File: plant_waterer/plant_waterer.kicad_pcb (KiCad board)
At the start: 2 copper layers, 59.1 x 41.3 mm, 20 parts, among them J1 PJ-002AH, J2 Conn_01x02, J3 Conn_01x03, U1 XIAO_RP2040, U2 TB6612FNG,C,8,EL, U3 OLED_DISP, U4 AP2204R-5.0TRG1

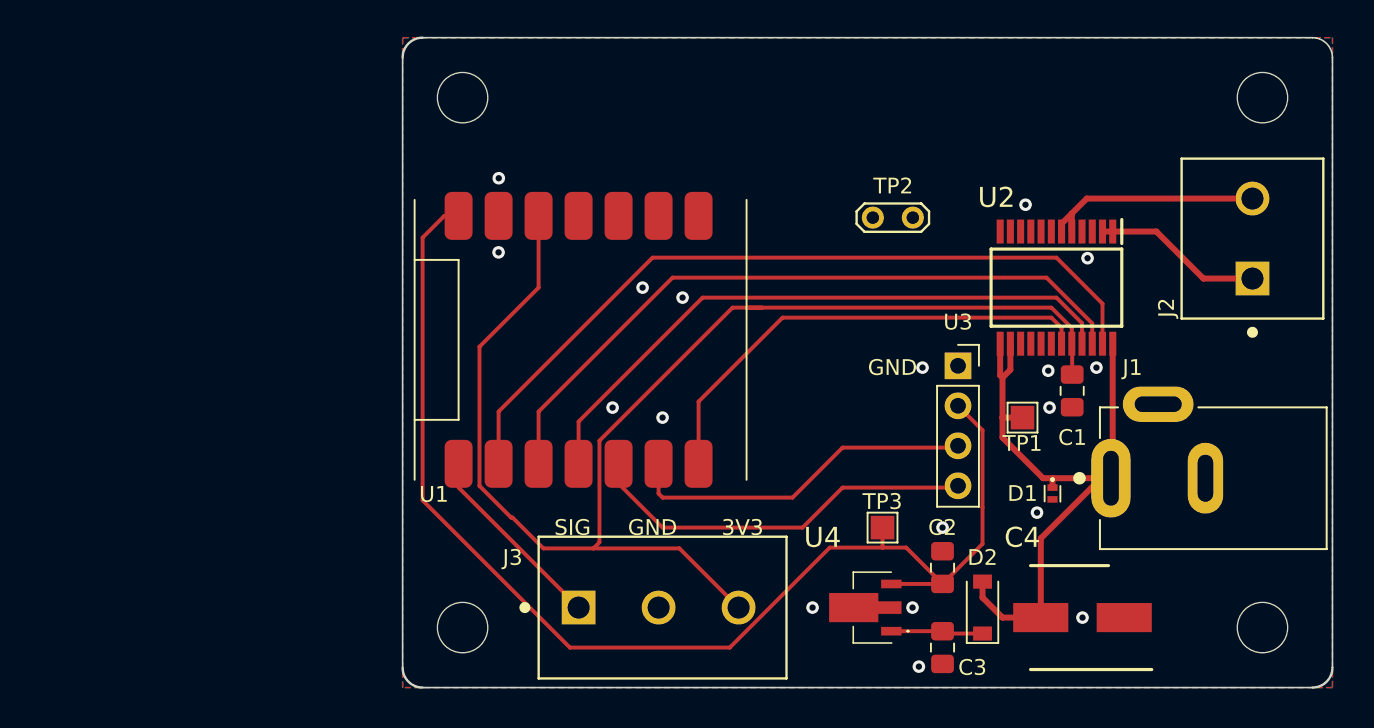
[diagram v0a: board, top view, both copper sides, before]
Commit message: Added UART input Added second motor output Added fuse and reverse polarity protection
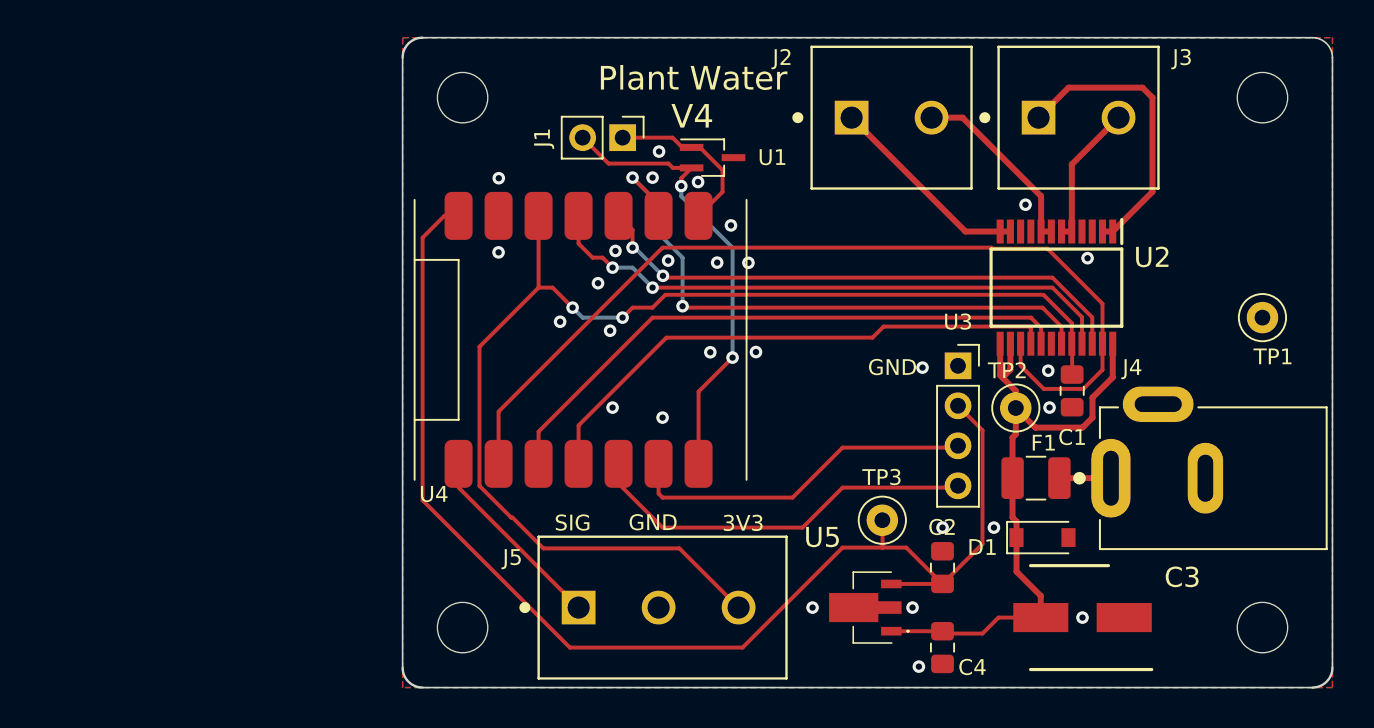
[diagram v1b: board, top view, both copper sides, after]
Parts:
- removed D2: D, Diode_SMD:D_SOD-123
- added F1: Polyfuse_Small, Fuse:Fuse_1210_3225Metric_Pad1.42x2.65mm_HandSolder, F.Cu at (101.2, 62.9)
- added J1: Conn_01x02, Connector_PinHeader_2.54mm:PinHeader_1x02_P2.54mm_Vertical, F.Cu at (74.9, 41.3)
- added J2: Conn_01x02, Library:CONN 1x2 5mm, F.Cu at (94.8, 40.0)
- added U1: ESD7002, Package_TO_SOT_SMD:SOT-323_SC-70_Handsoldering, F.Cu at (80.6, 42.5)
- D1: value SP3130-01ETG -> TV02W480-G; footprint Library:SP3130-01ETG -> Diode_SMD:D_SOD-123
- TP1: renamed from TP2; footprint TestPoint:TestPoint_2Pads_Pitch2.54mm_Drill0.8mm -> TestPoint:TestPoint_Loop_D1.80mm_Drill1.0mm_Beaded
- TP2: renamed from TP1; footprint TestPoint:TestPoint_Pad_1.5x1.5mm -> TestPoint:TestPoint_Loop_D1.80mm_Drill1.0mm_Beaded
- TP3: footprint TestPoint:TestPoint_Pad_1.5x1.5mm -> TestPoint:TestPoint_Loop_D1.80mm_Drill1.0mm_Beaded
- moved TP1 25.5 mm to (115.6, 52.7)
- moved J3 9.59 mm to (106.7, 40.0), turned to 0 degrees
- moved D1 3.24 mm to (101.6, 66.7), turned to 0 degrees
- moved TP2 0.74 mm to (99.9, 58.4)
- moved TP3 0.47 mm to (91.4, 65.6)
- renumbered C4 to C3, C3 to C4, J2 to J3, J1 to J4, J3 to J5, U1 to U4, U4 to U5
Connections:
- C4 pad 2: Net-(D2-Pad1) -> +12V
- J4 pad 1: +12V -> Net-(J1-Pad1)
- U2 pad 11: unconnected-(U3-Pad11) -> /B01
- U2 pad 12: unconnected-(U3-Pad12) -> /B01
- U2 pad 15: unconnected-(U3-Pad15) -> /PWMA
- U2 pad 16: unconnected-(U3-Pad16) -> /BIN2
- U2 pad 17: unconnected-(U3-Pad17) -> /BIN1
- U2 pad 7: unconnected-(U3-Pad7) -> /BO2
- U2 pad 8: unconnected-(U3-Pad8) -> /BO2
- U4 pad 10: unconnected-(U1-Pad10) -> /AIN1
- U4 pad 2: /AIN2 -> /BIN1
- U4 pad 3: /AIN1 -> /BIN2
- U4 pad 6: /STBY -> Net-(U1-Pad6)
- U4 pad 7: unconnected-(U1-Pad7) -> Net-(U1-Pad7)
- U4 pad 8: unconnected-(U1-Pad8) -> /STBY
- U4 pad 9: unconnected-(U1-Pad9) -> /AIN2
- U5 pad 1: Net-(D2-Pad1) -> +12V
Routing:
- net /BIN1: track 0.00 -> 38.2 mm
- net /BIN2: track 0.00 -> 34.8 mm
- net Net-(U1-Pad6): track 0.00 -> 29.0 mm, vias 0 -> 2
- net /B01: track 0.00 -> 13.1 mm
- net /BO2: track 0.00 -> 11.9 mm
- net /PWMA: track 49.5 -> 59.4 mm
- net Net-(U1-Pad7): track 0.00 -> 9.62 mm
- net /AIN2: track 44.5 -> 35.1 mm, vias 0 -> 2
- net /AO1: track 10.8 -> 18.5 mm
- net /STBY: track 30.5 -> 37.5 mm, vias 0 -> 2
- net Net-(D2-Pad1): track 5.85 -> 0.00 mm
- net +3.3V: track 83.4 -> 77.6 mm, vias 0 -> 2
- net /AO2: track 14.0 -> 9.11 mm
- net Net-(J1-Pad1): track 0.00 -> 3.27 mm
- net /AIN1: track 39.9 -> 37.4 mm, vias 0 -> 2
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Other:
- board text added: "Plant Water V4"

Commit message: Updated version to latest
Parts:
- moved TP1 3.42 mm to (112.4, 51.4)
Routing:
- net GND: vias 28 -> 35
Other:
- board text added: "12V 250mA"
- board text added: "Plant Water V5"
- board text removed: "Plant Water V4"
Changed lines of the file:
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@@
     (fp_line (start 1.6 1.25) (end -1.6 1.25) (layer "F.Fab") (width 0.1))
     (fp_line (start 1.6 -1.25) (end 1.6 1.25) (layer "F.Fab") (width 0.1))
-    (pad "1" smd roundrect (at -1.4875 0 180) (size 1.425 2.65) (layers "F.Cu" "F.Paste" "F.Mask") (roundrect_rratio 0.175439)
+    (pad "1" smd roundrect (at -1.4875 0 180) (size 1.425 2.65) (layers "F.Cu" "F.Paste" "F.Mask") (roundrect_rratio 0.1754392982)
       (net 16 "Net-(J1-Pad1)") (pintype "passive"))
-    (pad "2" smd roundrect (at 1.4875 0 180) (size 1.425 2.65) (layers "F.Cu" "F.Paste" "F.Mask") (roundrect_rratio 0.175439)
+    (pad "2" smd roundrect (at 1.4875 0 180) (size 1.425 2.65) (layers "F.Cu" "F.Paste" "F.Mask") (roundrect_rratio 0.1754392982)
       (net 3 "+12V") (pintype "passive"))
     (model "${KICAD6_3DMODEL_DIR}/Fuse.3dshapes/Fuse_1210_3225Metric.wrl"
@@
   )
   (footprint "TestPoint:TestPoint_Loop_D1.80mm_Drill1.0mm_Beaded" (layer "F.Cu")
-    (at 115.57 52.705)
+    (at 112.395 51.435)
     (descr "wire loop with bead as test point, loop diameter 1.8mm, hole diameter 1.0mm")
     (tags "test point wire loop bead")
@@
     (effects (font (size 1 1) (thickness 0.15)))
   )
-  (gr_text "Plant Water\nV4" (at 79.375 38.735) (layer "F.SilkS")
+  (gr_text "Plant Water\nV5" (at 79.375 38.735) (layer "F.SilkS")
     (effects (font (size 1.5 1.5) (thickness 0.3)))
   )
   (gr_text "GND" (at 92.075 55.88) (layer "F.SilkS")
+    (effects (font (size 1 1) (thickness 0.15)))
+  )
+  (gr_text "12V 250mA" (at 118.745 53.34 90) (layer "F.SilkS")
     (effects (font (size 1 1) (thickness 0.15)))
   )
@@
   (via (at 93.748867 74.869654) (size 0.8) (drill 0.4) (layers "F.Cu" "B.Cu") (free) (net 1))
   (via (at 101.964058 56.077174) (size 0.8) (drill 0.4) (layers "F.Cu" "B.Cu") (free) (net 1))
+  (via (at 96.816593 74.839758) (size 0.8) (drill 0.4) (layers "F.Cu" "B.Cu") (free) (net 1))
   (via (at 102.046359 58.416855) (size 0.8) (drill 0.4) (layers "F.Cu" "B.Cu") (free) (net 1))
   (via (at 86.995 71.12) (size 0.8) (drill 0.4) (layers "F.Cu" "B.Cu") (free) (net 1))
@@
   (via (at 76.835 43.815) (size 0.8) (drill 0.4) (layers "F.Cu" "B.Cu") (free) (net 1))
   (via (at 74.4806 48.471006) (size 0.8) (drill 0.4) (layers "F.Cu" "B.Cu") (free) (net 1))
+  (via (at 100.539658 48.699476) (size 0.8) (drill 0.4) (layers "F.Cu" "B.Cu") (free) (net 1))
   (via (at 79.725295 44.093377) (size 0.8) (drill 0.4) (layers "F.Cu" "B.Cu") (free) (net 1))
   (via (at 77.47 59.055) (size 0.8) (drill 0.4) (layers "F.Cu" "B.Cu") (free) (net 1))
+  (via (at 104.450136 45.525972) (size 0.8) (drill 0.4) (layers "F.Cu" "B.Cu") (free) (net 1))
+  (via (at 82.169779 41.568877) (size 0.8) (drill 0.4) (layers "F.Cu" "B.Cu") (free) (net 1))
+  (via (at 101.902302 66.685827) (size 0.8) (drill 0.4) (layers "F.Cu" "B.Cu") (free) (net 1))
   (via (at 67.053675 48.560428) (size 0.8) (drill 0.4) (layers "F.Cu" "B.Cu") (free) (net 1))
   (via (at 83.40105 54.8908) (size 0.8) (drill 0.4) (layers "F.Cu" "B.Cu") (free) (net 1))
@@
   (via (at 82.92496 49.223992) (size 0.8) (drill 0.4) (layers "F.Cu" "B.Cu") (free) (net 1))
   (via (at 93.345 71.12) (size 0.8) (drill 0.4) (layers "F.Cu" "B.Cu") (free) (net 1))
+  (via (at 104.414032 66.700867) (size 0.8) (drill 0.4) (layers "F.Cu" "B.Cu") (free) (net 1))
   (via (at 77.247722 42.158226) (size 0.8) (drill 0.4) (layers "F.Cu" "B.Cu") (free) (net 1))
+  (via (at 82.2149 43.554196) (size 0.8) (drill 0.4) (layers "F.Cu" "B.Cu") (free) (net 1))
   (via (at 73.370251 50.52088) (size 0.8) (drill 0.4) (layers "F.Cu" "B.Cu") (free) (net 1))
   (via (at 67.067607 43.851813) (size 0.8) (drill 0.4) (layers "F.Cu" "B.Cu") (free) (net 1))
@@
   (segment (start 76.835 50.8) (end 75.565 49.53) (width 0.25) (layer "B.Cu") (net 9))
   (segment (start 75.565 49.53) (end 74.295 49.53) (width 0.25) (layer "B.Cu") (net 9))
+  (segment (start 93.345 48.26) (end 77.47 48.26) (width 0.25) (layer "F.Cu") (net 10))
+  (segment (start 103.12 49.53) (end 94.615 49.53) (width 0.25) (layer "F.Cu") (net 10))
+  (segment (start 105.41 54.362) (end 105.41 51.82) (width 0.25) (layer "F.Cu") (net 10))
+  (segment (start 77.47 48.26) (end 67.056 58.674) (width 0.25) (layer "F.Cu") (net 10))
   (segment (start 100.21 55.76) (end 100.21 54.362) (width 0.25) (layer "F.Cu") (net 10))
   (segment (start 105.41 54.362) (end 105.41 56.020346) (width 0.25) (layer "F.Cu") (net 10))
-  (segment (start 77.47 48.26) (end 67.056 58.674) (width 0.25) (layer "F.Cu") (net 10))
-  (segment (start 101.9155 48.3255) (end 98.4255 48.3255) (width 0.25) (layer "F.Cu") (net 10))
   (segment (start 101.683115 57.233115) (end 100.21 55.76) (width 0.25) (layer "F.Cu") (net 10))
-  (segment (start 67.056 58.674) (end 67.056 61.991969) (width 0.25) (layer "F.Cu") (net 10))
+  (segment (start 94.615 49.53) (end 93.345 48.26) (width 0.25) (layer "F.Cu") (net 10))
   (segment (start 104.197231 57.233115) (end 101.683115 57.233115) (width 0.25) (layer "F.Cu") (net 10))
   (segment (start 105.41 56.020346) (end 104.197231 57.233115) (width 0.25) (layer "F.Cu") (net 10))
-  (segment (start 98.36 48.26) (end 77.47 48.26) (width 0.25) (layer "F.Cu") (net 10))
-  (segment (start 105.41 51.82) (end 101.9155 48.3255) (width 0.25) (layer "F.Cu") (net 10))
-  (segment (start 105.41 54.362) (end 105.41 51.82) (width 0.25) (layer "F.Cu") (net 10))
-  (segment (start 98.4255 48.3255) (end 98.36 48.26) (width 0.25) (layer "F.Cu") (net 10))
+  (segment (start 105.41 51.82) (end 103.12 49.53) (width 0.25) (layer "F.Cu") (net 10))
+  (segment (start 67.056 58.674) (end 67.056 61.991969) (width 0.25) (layer "F.Cu") (net 10))
   (segment (start 101.6 52.07) (end 102.81 53.28) (width 0.25) (layer "F.Cu") (net 11))
   (segment (start 78.8295 52.07) (end 101.6 52.07) (width 0.25) (layer "F.Cu") (net 11))

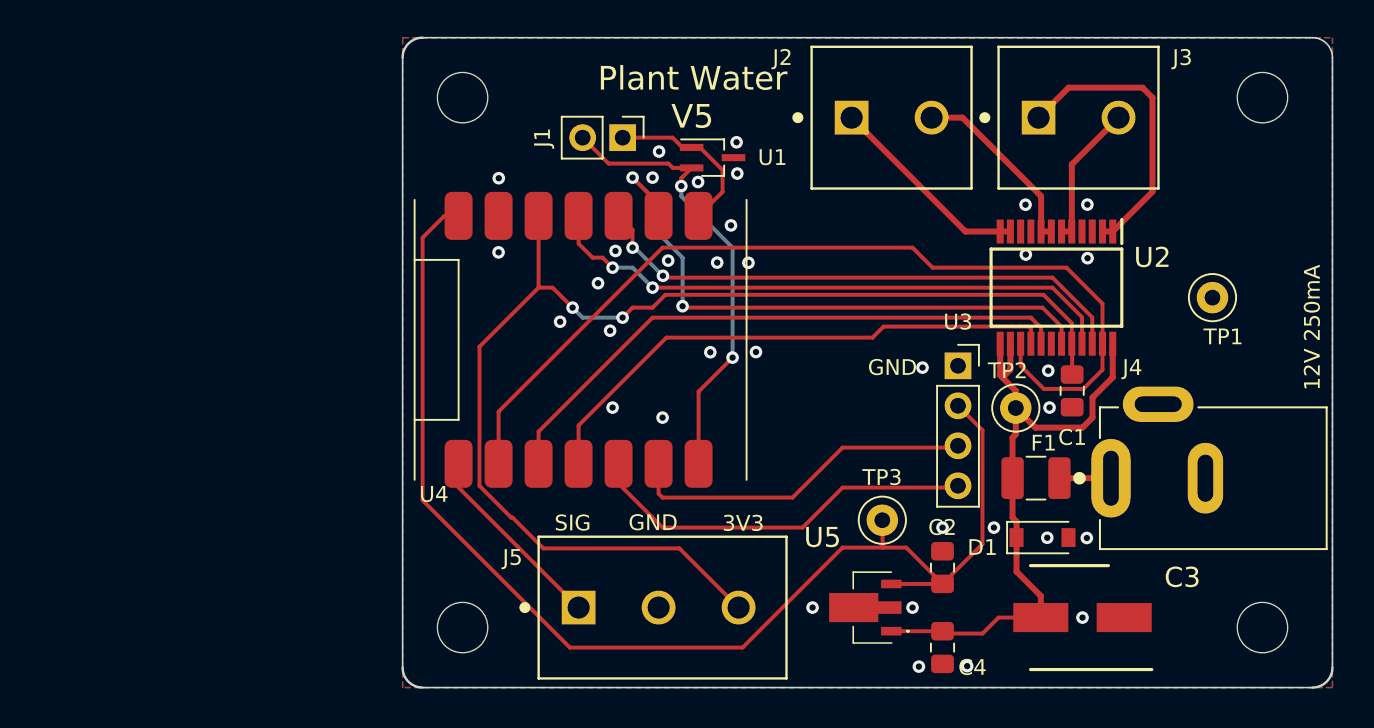
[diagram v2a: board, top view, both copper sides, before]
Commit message: Add adjustable level set Add power filtering Add ESD
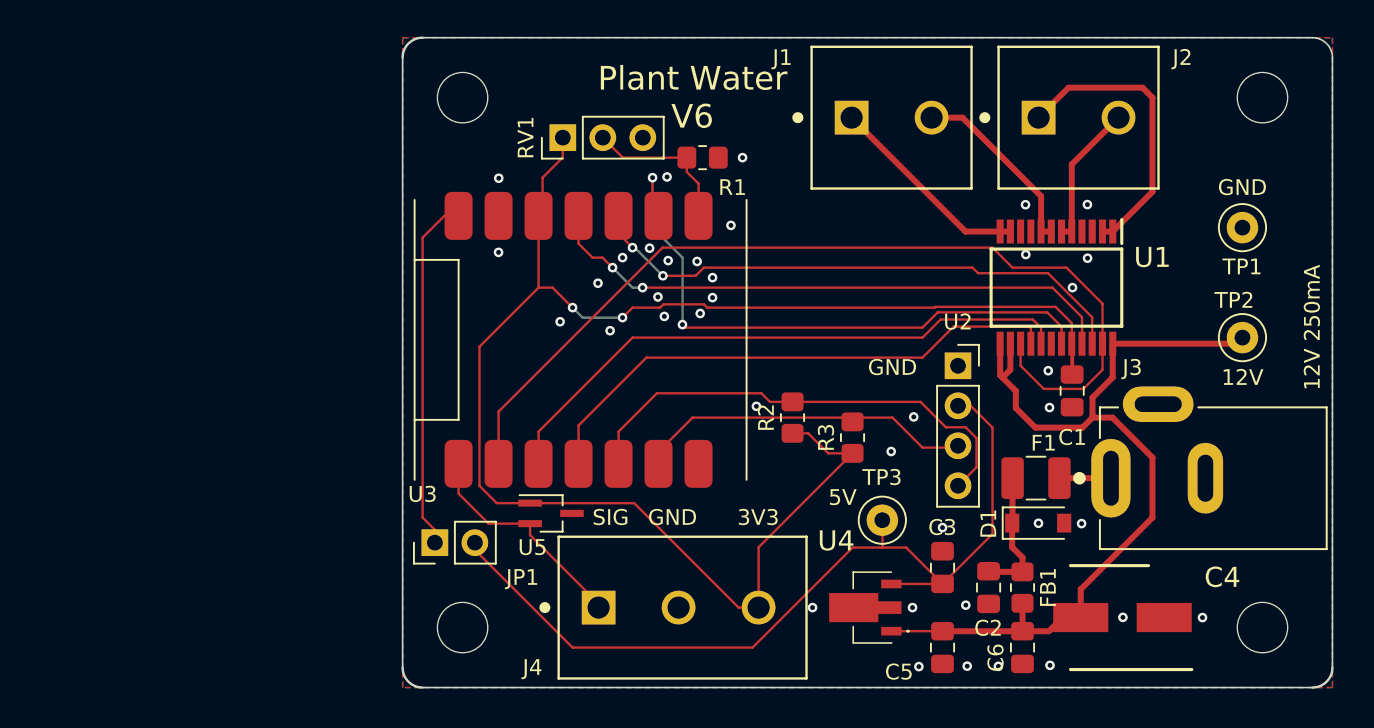
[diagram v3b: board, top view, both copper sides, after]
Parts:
- removed the J1 at (74.9, 41.3)
- removed the U1 at (80.6, 42.5)
- added C2: 1uF, Capacitor_SMD:C_0805_2012Metric_Pad1.18x1.45mm_HandSolder, F.Cu at (98.2, 69.8)
- added C6: 1uF, Capacitor_SMD:C_0805_2012Metric_Pad1.18x1.45mm_HandSolder, F.Cu at (100.3, 73.7)
- added FB1: ACML-0805-601-T, Resistor_SMD:R_0805_2012Metric_Pad1.20x1.40mm_HandSolder, F.Cu at (100.3, 69.8)
- added JP1: Jumper_2_Bridged, Connector_PinHeader_2.54mm:PinHeader_1x02_P2.54mm_Vertical, F.Cu at (63.0, 67.0)
- added R1: 10K, Resistor_SMD:R_0805_2012Metric_Pad1.20x1.40mm_HandSolder, F.Cu at (80.0, 42.5)
- added R2: 10K, Resistor_SMD:R_0805_2012Metric_Pad1.20x1.40mm_HandSolder, F.Cu at (85.7, 59.1)
- added R3: 10K, Resistor_SMD:R_0805_2012Metric_Pad1.20x1.40mm_HandSolder, F.Cu at (89.5, 60.3)
- added RV1: 100K, Connector_PinHeader_2.54mm:PinHeader_1x03_P2.54mm_Vertical, F.Cu at (71.1, 41.3)
- added U5: ESD7002, Package_TO_SOT_SMD:SOT-323_SC-70_Handsoldering, F.Cu at (70.4, 65.1)
- moved TP2 15.1 mm to (114.3, 54.0)
- moved TP1 4.84 mm to (114.3, 47.0)
- moved C4 2.54 mm to (106.7, 71.8)
- moved J4 1.27 mm to (78.7, 71.1)
- moved D1 0.96 mm to (101.3, 65.8)
- renumbered C2 to C3, C3 to C4, C4 to C5, J2 to J1, J3 to J2, J4 to J3, J5 to J4, U2 to U1, U3 to U2, U4 to U3, U5 to U4
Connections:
- D1 pad 1: +12V -> /VIN
- F1 pad 2: +12V -> /VIN
- U3 pad 13: +5V -> Net-(U3-Pad13)
- U3 pad 6: Net-(U1-Pad6) -> unconnected-(U3-Pad6)
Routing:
- net Net-(U1-Pad6): track 29.0 -> 0.00 mm, vias 2 -> 0
- net +5V: track 77.5 -> 54.8 mm
- net Net-(U3-Pad13): track 0.00 -> 22.6 mm
- net +3.3V: track 77.6 -> 100.0 mm
- net +12V: track 41.6 -> 57.2 mm
- net /VIN: track 0.00 -> 7.86 mm
- net Net-(U2-Pad4): track 23.7 -> 30.5 mm
- net Net-(J4-Pad1): track 12.3 -> 14.4 mm
- net Net-(U2-Pad3): track 22.2 -> 21.4 mm
- net GND: vias 35 -> 39
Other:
- board text added: "12V"
- board text added: "5V"
- board text added: "Plant Water V6"
- board text removed: "Plant Water V5"

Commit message: Minor clean up and adding schmatic
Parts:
- renumbered C3 to C2, C2 to C3, U5 to U4, U4 to U5
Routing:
- net /PWMA: track 59.4 -> 60.0 mm
- net GND: vias 39 -> 38
